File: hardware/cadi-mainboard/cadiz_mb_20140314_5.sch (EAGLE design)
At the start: 82 parts, among them T1 FDS6680A, T2 FDS6680A, T3 FDS6680A, T4 FDS6680A, T5 FDS6680A, T6 FDS6680A, T7 FDS6680A, T8 FDS6680A

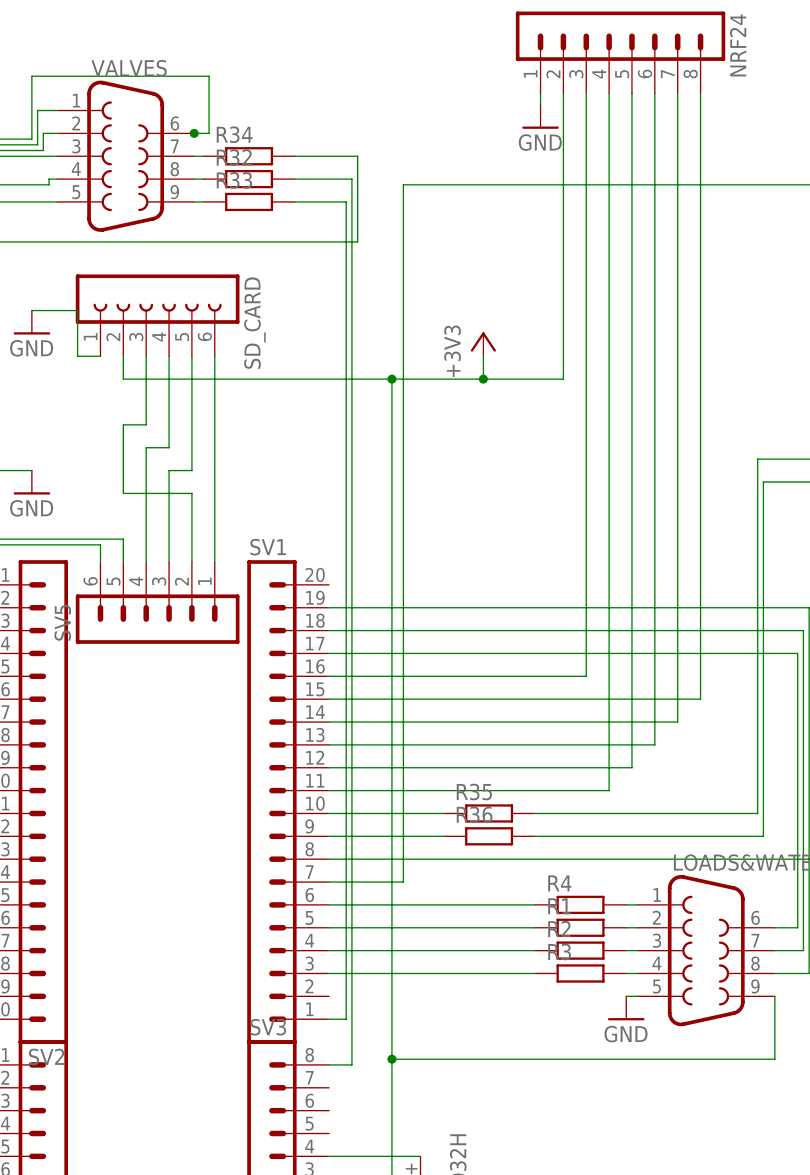
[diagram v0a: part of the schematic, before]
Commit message: adc and dht rework
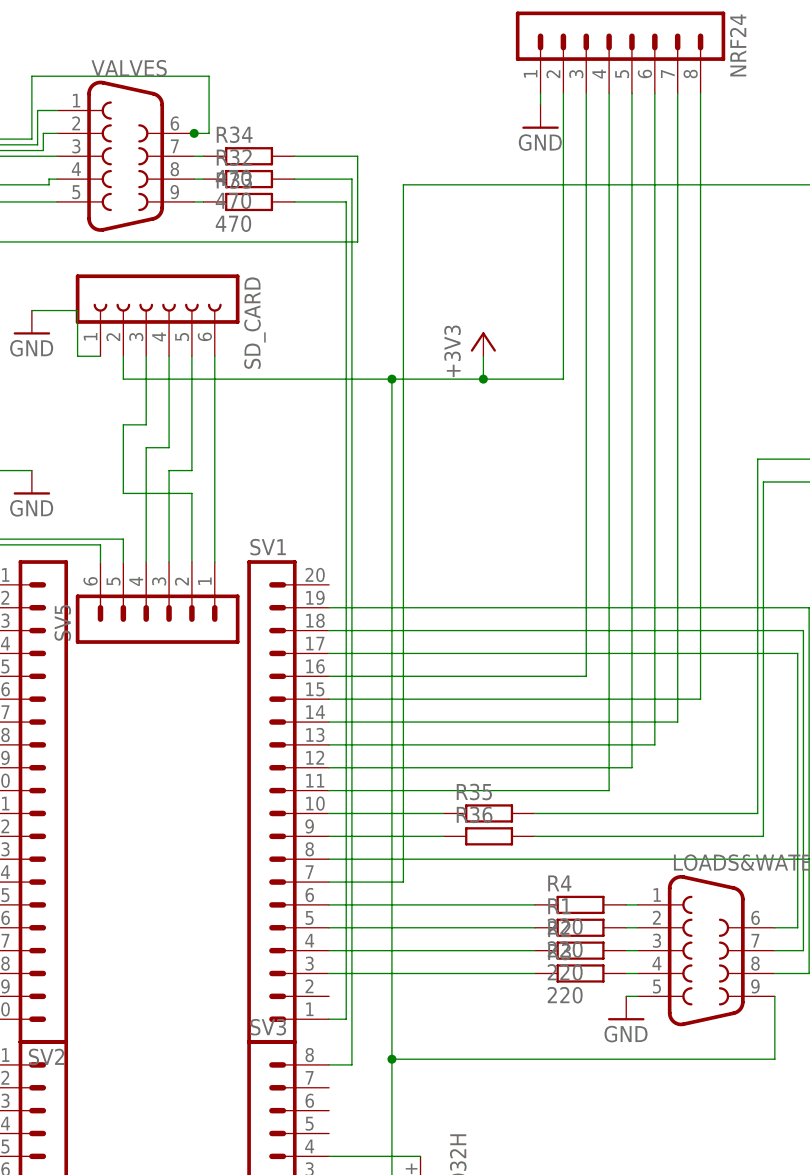
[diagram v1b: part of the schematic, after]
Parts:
- R1, R2, R3, R4: value (none) -> 220
- R32, R33, R34: value (none) -> 470
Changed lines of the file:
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@@
 <part name="GND9" library="supply1" deviceset="GND" device=""/>
 <part name="T1" library="FDS6680A" deviceset="FDS6680A_SOP8" device="" value="FDS6680A"/>
-<part name="R1" library="resistor" deviceset="R-EU_" device="M1206"/>
-<part name="R2" library="resistor" deviceset="R-EU_" device="M1206"/>
-<part name="R3" library="resistor" deviceset="R-EU_" device="M1206"/>
-<part name="R4" library="resistor" deviceset="R-EU_" device="M1206"/>
+<part name="R1" library="resistor" deviceset="R-EU_" device="M1206" value="220"/>
+<part name="R2" library="resistor" deviceset="R-EU_" device="M1206" value="220"/>
+<part name="R3" library="resistor" deviceset="R-EU_" device="M1206" value="220"/>
+<part name="R4" library="resistor" deviceset="R-EU_" device="M1206" value="220"/>
 <part name="VT1" library="transistor" deviceset="BC847" device="" value="3904"/>
 <part name="R5" library="resistor" deviceset="R-EU_" device="M1206" value="100"/>
@@
 <part name="GND28" library="supply1" deviceset="GND" device=""/>
 <part name="P+1" library="supply1" deviceset="+5V" device=""/>
-<part name="R32" library="resistor" deviceset="R-EU_" device="M1206"/>
-<part name="R33" library="resistor" deviceset="R-EU_" device="M1206"/>
-<part name="R34" library="resistor" deviceset="R-EU_" device="M1206"/>
+<part name="R32" library="resistor" deviceset="R-EU_" device="M1206" value="470"/>
+<part name="R33" library="resistor" deviceset="R-EU_" device="M1206" value="470"/>
+<part name="R34" library="resistor" deviceset="R-EU_" device="M1206" value="470"/>
 <part name="P+2" library="supply1" deviceset="+5V" device=""/>
 <part name="BLUETOOTH_UART" library="con-lstb" deviceset="MA04-1" device=""/>
